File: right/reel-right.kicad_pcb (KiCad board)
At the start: 2 copper layers, 134 x 86.9 mm, 46 parts, among them J1 Conn_01x02, SW1 SW_Push, SW10 SW_Push, SW11 SW_Push, SW12 SW_Push, SW13 SW_Push, SW14 SW_Push, SW15 SW_Push, SW16 SW_Push, SW17 SW_Push, SW18 SW_Push, SW19 SW_Push, SW2 SW_Push, SW22 SW_SPDT, SW3 SW_Push, SW4 SW_Push, SW5 SW_Push, SW6 SW_Push, SW7 SW_Push, SW8 SW_Push, SW9 SW_Push

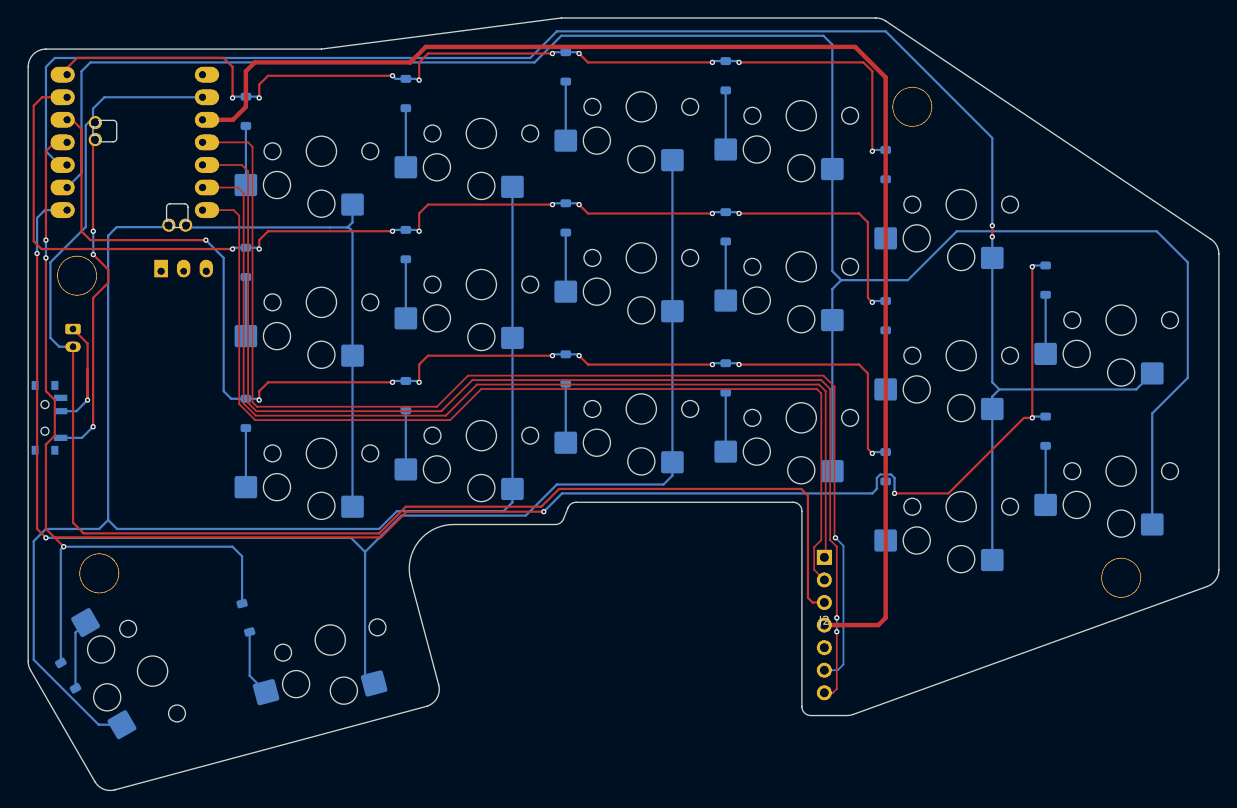
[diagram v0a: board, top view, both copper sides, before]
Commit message: Update ReeL KiCad board files
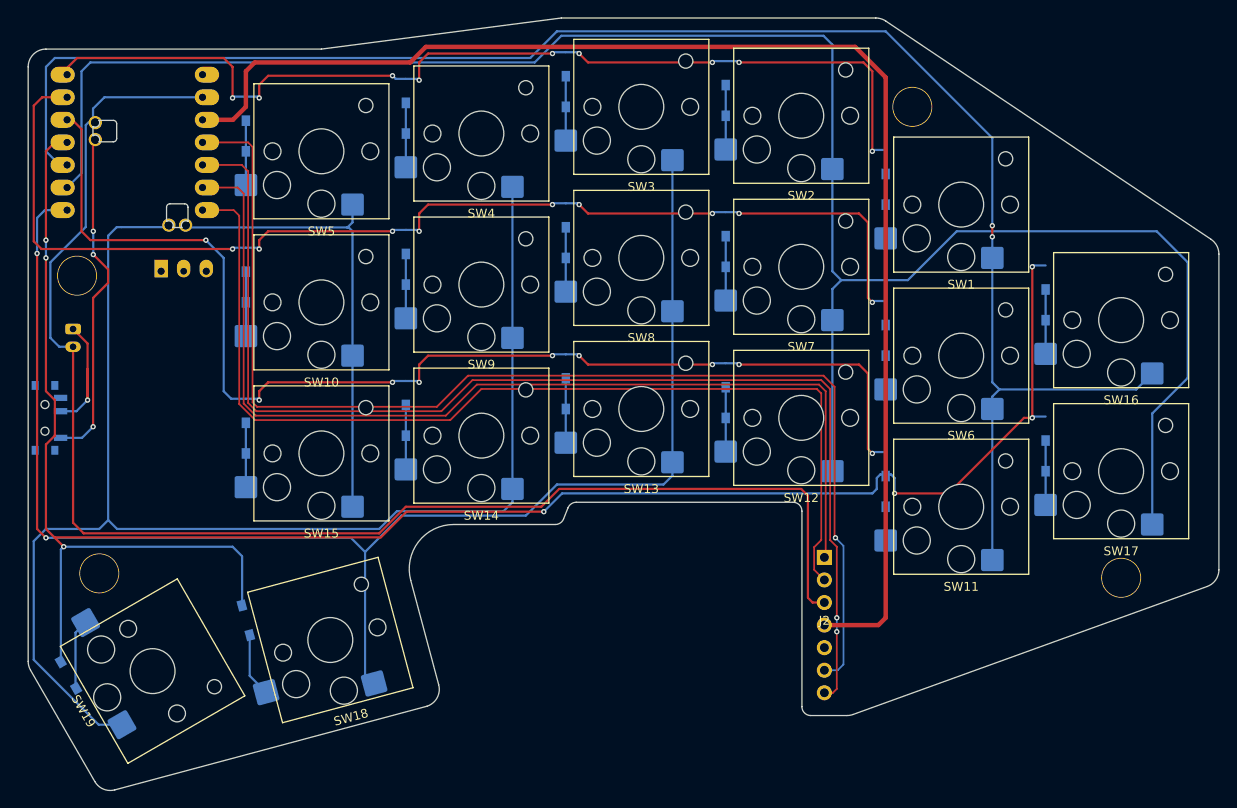
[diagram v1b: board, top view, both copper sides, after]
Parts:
- D1, D10, D11, D12, D13, D14, D15, D16, D17, D18, D19, D2, D3, D4, D5, D6, D7, D8, D9: footprint Diode_SMD:D_SOD-123 -> reel:Diode_SMD; moved to F.Cu
- SW1, SW10, SW11, SW12, SW13, SW14, SW15, SW16, SW17, SW18, SW19, SW2, SW3, SW4, SW5, SW6, SW7, SW8, SW9: footprint reel:SW_Hotswap_Kailh_Choc_V1_1.00u-NoClickHole -> reel:SW_Hotswap_Kailh_Choc_V1V2_1.00u
- moved D19 2.80 mm to (50.1, 117.0)
- moved D18 2.51 mm to (70.8, 110.6)

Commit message: Update ReeL KiCad board files
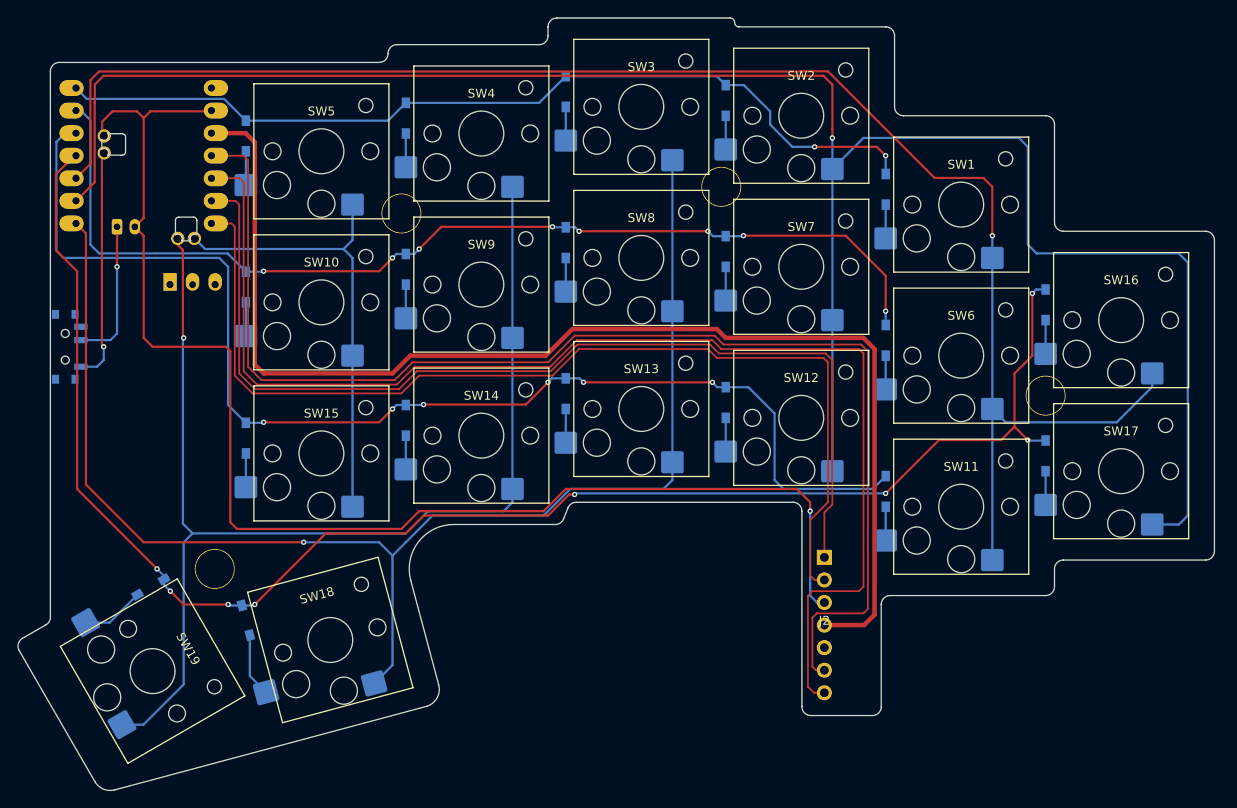
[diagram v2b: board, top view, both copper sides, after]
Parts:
- removed the Ref** at (146.5, 55.5)
- removed the Ref** at (52.5, 74.5)
- removed the Ref** at (170.0, 108.5)
- added Ref**: Val**, reel:m2_Spacer_Hole, F.Cu at (161.5, 88.0)
- added Ref**: Val**, reel:m2_Spacer_Hole, F.Cu at (89.0, 67.5)
- added Ref**: Val**, reel:m2_Spacer_Hole, F.Cu at (68.0, 107.5)
- moved Ref** 82.4 mm to (125.0, 64.5)
- moved D19 15.8 mm to (63.2, 108.1), turned to -150 degrees
- moved J1 12.5 mm to (57.0, 69.0), turned to 0 degrees
- moved SW22 8.32 mm to (51.5, 82.5)
- moved U1 1.80 mm to (60.0, 50.5)
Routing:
- net Row3: track 227.3 -> 181.1 mm, vias 7 -> 8
- net Col3: track 157.3 -> 132.6 mm, vias 0 -> 1
- net Row1: track 129.6 -> 116.8 mm, vias 9 -> 8
- net 3.3V: track 152.1 -> 139.5 mm
- net Col2: track 166.1 -> 153.9 mm, vias 2 -> 1
- net GND: track 162.2 -> 150.5 mm, vias 0 -> 1
- net VBAT_SW: track 37.7 -> 26.1 mm, vias 3 -> 1
- net Row0: track 112.1 -> 101.4 mm, vias 9 -> 2
- net Col0: track 191.8 -> 182.8 mm, vias 2 -> 1
- net MOTION: track 134.9 -> 143.4 mm, vias 2 -> 0
- net SDIO: track 136.3 -> 143.4 mm, vias 1 -> 0
- net Col1: track 223.0 -> 227.9 mm, vias 0 -> 1
- net Row2: track 134.6 -> 137.5 mm, vias 9 -> 6
- net Net-(D5-A): track 6.65 -> 3.80 mm
- net Net-(D4-A): track 6.65 -> 3.80 mm
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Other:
- board size 134 x 86.9 mm -> 134.6 x 86.9 mm

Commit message: Update PCB layouts and fabrication outputs
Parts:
- moved J1 6.80 mm to (59.0, 75.5), turned to 180 degrees
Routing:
- net (no net): track 0.00 -> 5.47 mm
- net GND: track 150.5 -> 155.4 mm
- net Net-(J1-Pin_1): track 16.4 -> 11.7 mm, vias 1 -> 0

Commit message: Route right Col3 trace
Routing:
- net (no net): track 5.47 -> 0.00 mm
- net Col3: track 132.6 -> 137.1 mm
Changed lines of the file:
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@@
-	)
-	(segment
-		(start 70.5 92)
-		(end 70.5 86.777818)
-		(width 0.5)
-		(layer "F.Cu")
-		(net "")
-	)
-	(segment
-		(start 70.5 86.777818)
-		(end 70.325 86.602818)
-		(width 0.5)
-		(layer "F.Cu")
-		(net "")
 	)
 	(segment
@@
 	)
 	(segment
-		(start 64.5 81.5)
-		(end 64.413 81.413)
+		(start 69 73)
+		(end 65.717597 73)
 		(width 0.25)
 		(layer "F.Cu")
@@
 	)
 	(segment
-		(start 64.413 81.413)
-		(end 64.413 71.616589)
+		(start 69.5 80.5)
+		(end 69.5 73.5)
 		(width 0.25)
 		(layer "F.Cu")
@@
 		(net "Col3")
 	)
-	(via
-		(at 64.5 81.5)
+	(segment
+		(start 65.717597 73)
+		(end 63.748373 71.030776)
+		(width 0.25)
+		(layer "F.Cu")
+		(net "Col3")
+	)
+	(segment
+		(start 68.5 81.5)
+		(end 69.5 80.5)
+		(width 0.25)
+		(layer "F.Cu")
+		(net "Col3")
+	)
+	(segment
+		(start 69.5 73.5)
+		(end 69 73)
+		(width 0.25)
+		(layer "F.Cu")
+		(net "Col3")
+	)
+	(via
+		(at 68.5 81.5)
 		(size 0.6)
 		(drill 0.3)
@@
 	)
 	(segment
-		(start 64.413 102.413)
-		(end 64.413 81.587)
+		(start 68.5 102)
+		(end 68.5 81.5)
+		(width 0.25)
+		(layer "B.Cu")
+		(net "Col3")
+	)
+	(segment
+		(start 68.5 102)
+		(end 67 103.5)
 		(width 0.25)
 		(layer "B.Cu")
@@
 	)
 	(segment
+		(start 70 103.5)
+		(end 89.5 103.5)
+		(width 0.25)
+		(layer "B.Cu")
+		(net "Col3")
+	)
+	(segment
 		(start 101.5 64.5)
 		(end 101.5 81.5)
@@
 	)
 	(segment
-		(start 64.413 81.587)
-		(end 64.5 81.5)
+		(start 70 103.5)
+		(end 68.5 102)
 		(width 0.25)
 		(layer "B.Cu")
@@
 	(segment
 		(start 65.5 103.5)
-		(end 89.5 103.5)
-		(width 0.25)
-		(layer "B.Cu")
-		(net "Col3")
-	)
-	(segment
-		(start 65.5 103.5)
-		(end 64.413 102.413)
-		(width 0.25)
-		(layer "B.Cu")
+		(end 67 103.5)
+		(width 0.25)
+		(layer "B.Cu")
